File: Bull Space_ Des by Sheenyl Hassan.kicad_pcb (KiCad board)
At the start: 2 copper layers, 45 x 77 mm, 36 parts, among them IC1 TEENSY_4.0, IC2 XB24CZ7PIT-004, J1 Screw_Terminal_01x06, Q1 AOI21357, Q2 2N7002, Q3 2N7002, Q4 2N7002, Q5 AOI21357, U1 VXO7803-1000, U2 Flight-Computer_Adafruit_GPS_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

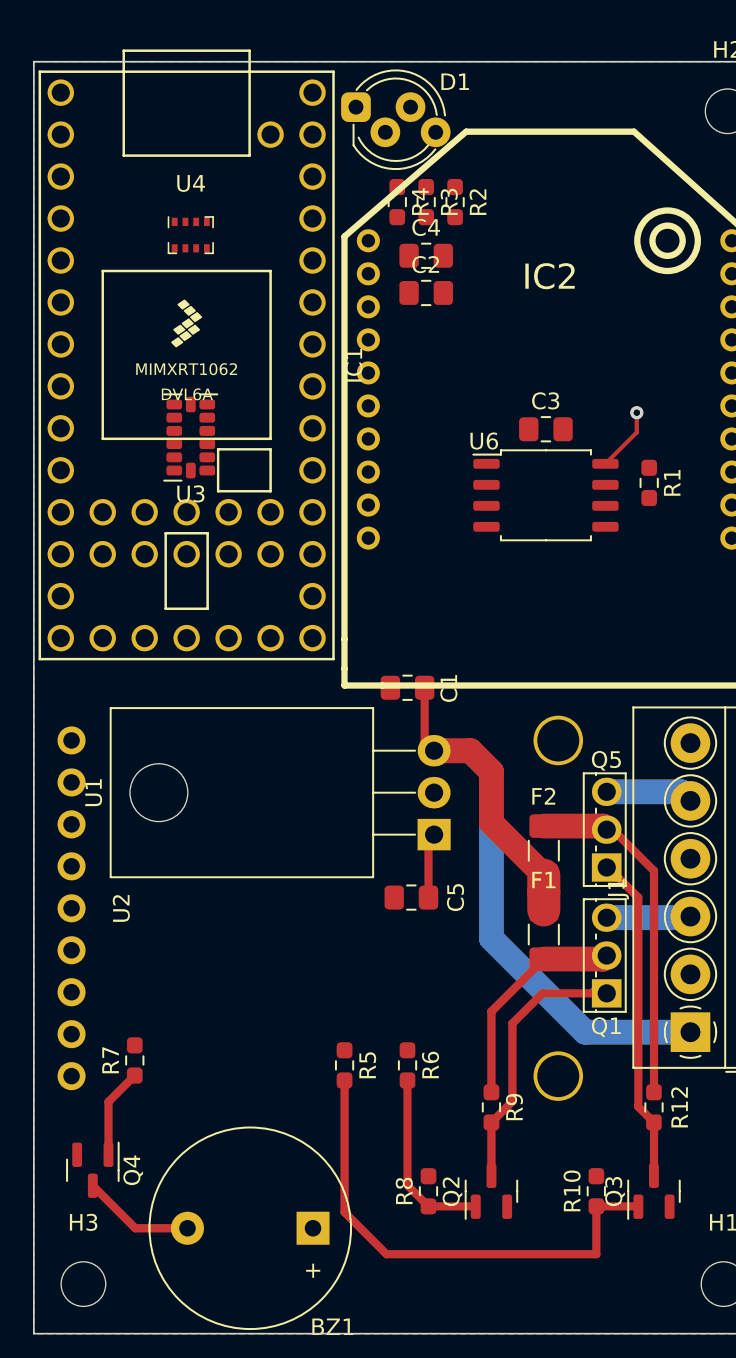
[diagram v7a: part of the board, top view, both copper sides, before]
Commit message: Tried to wire SPI
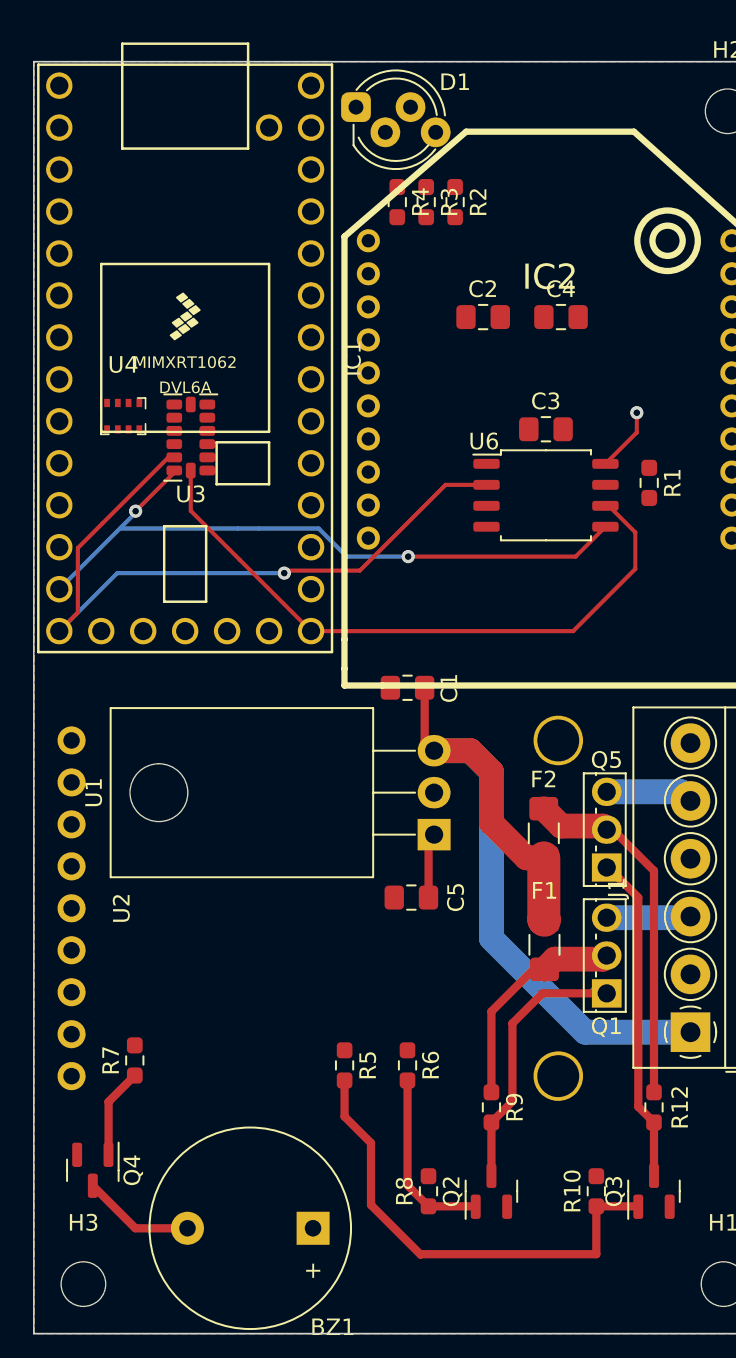
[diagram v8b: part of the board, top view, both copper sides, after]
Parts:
- moved U4 11.7 mm to (77.4, 85.5)
- moved C4 8.96 mm to (103.9, 79.5)
- moved C2 3.74 mm to (99.2, 79.5)
- moved F2 1.05 mm to (102.9, 110.7)
- moved F1 0.62 mm to (102.9, 117.5)
- moved IC1 0.43 mm to (81.2, 82.0)
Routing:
- net /MISO: track 0.00 -> 43.1 mm, vias 0 -> 1
- net /MOSI: track 0.00 -> 40.9 mm, vias 0 -> 2
- net /SCK: track 0.00 -> 38.6 mm
- net +BATT: track 46.2 -> 47.5 mm
- net Net-(Q3-Pad1): track 29.7 -> 28.5 mm
